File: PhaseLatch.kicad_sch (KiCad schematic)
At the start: 124 parts, among them J2 NC, J20 I_IN, J21 Q_IN, J23 CLK_IN, J5 Databus, J6 Chip select, J7 Addressbus, J8 Signals, P1 Conn_02x10_Odd_Even, P2 Conn_02x10_Odd_Even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

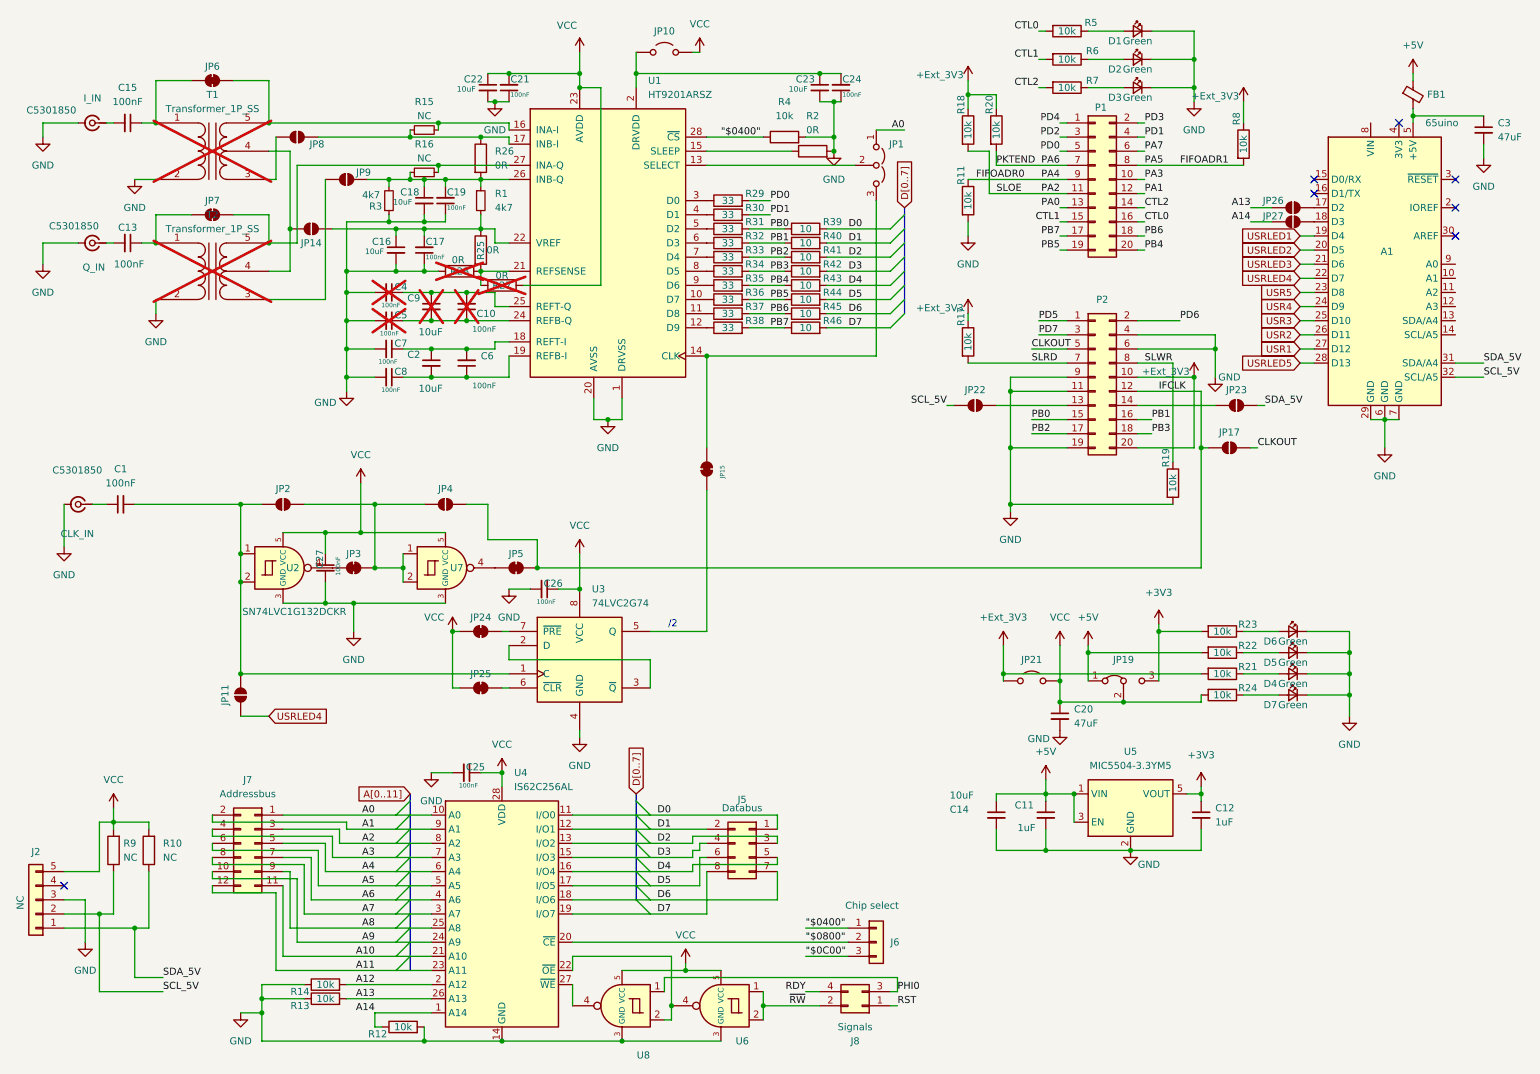
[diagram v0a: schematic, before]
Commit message: IQ bias offset, IQ balancing, documentation
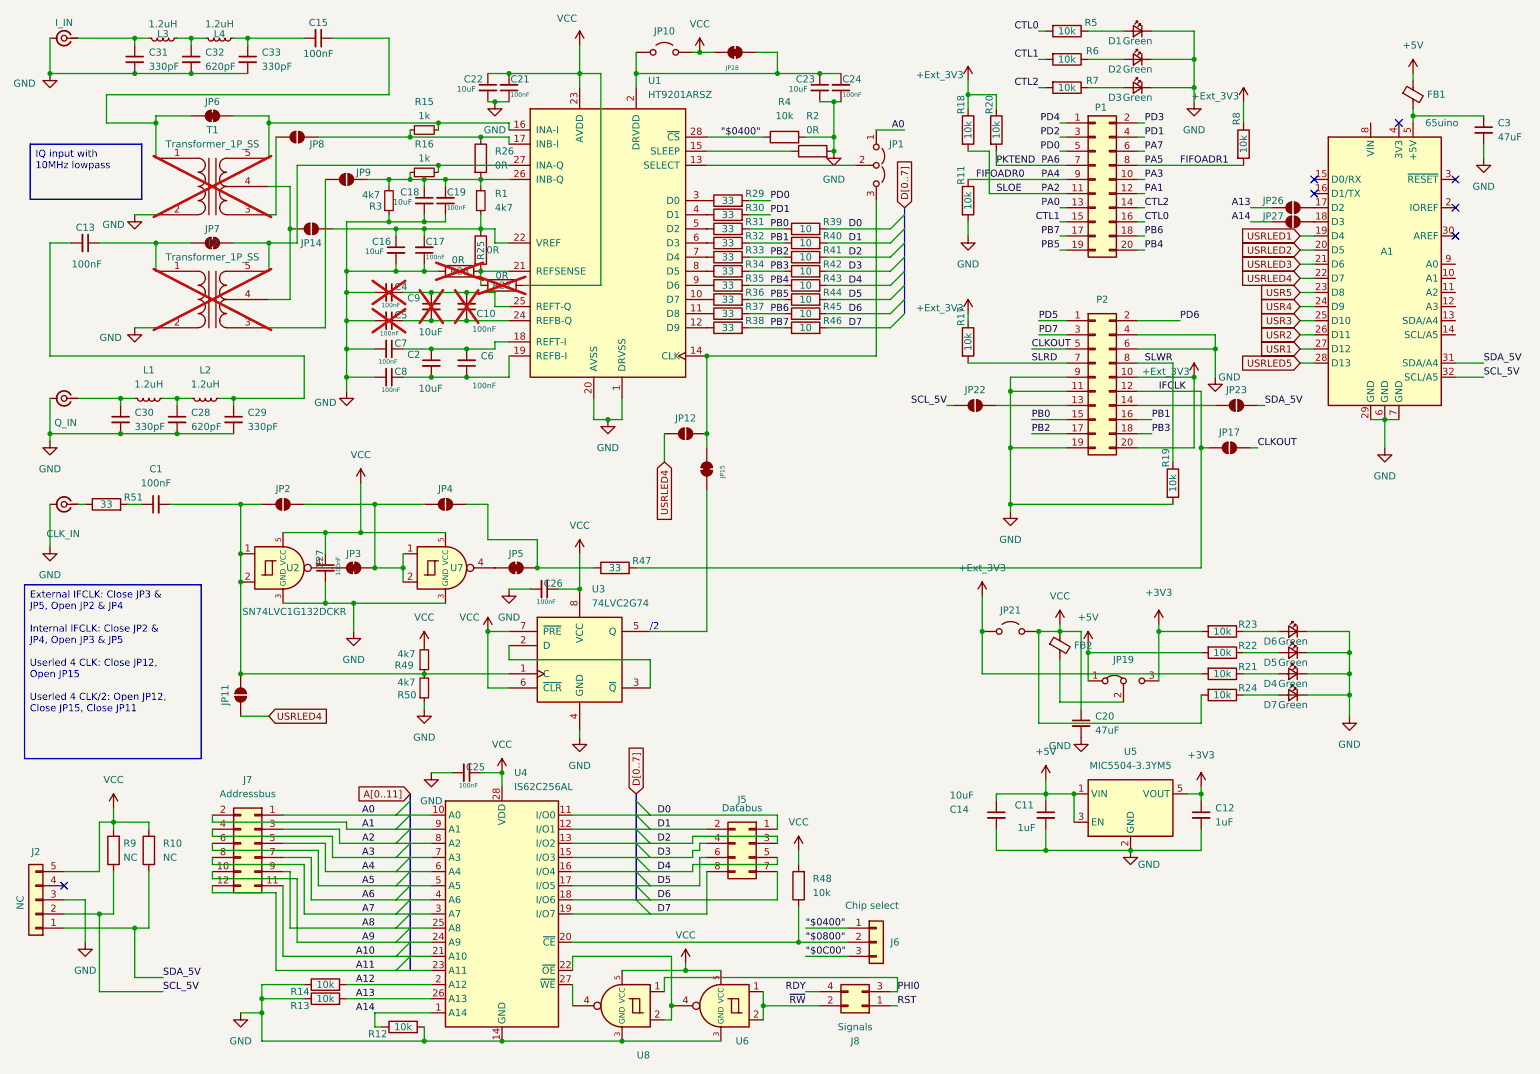
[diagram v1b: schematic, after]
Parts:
- removed JP24, JP25: ~, Jumper:SolderJumper-2_P1.3mm_Bridged_RoundedPad1.0x1.5mm, symbol Jumper:SolderJumper_2_Bridged
- added C28, C32: 620pF, Capacitor_SMD:C_0402_1005Metric, symbol Device:C_Small
- added C29, C30, C31, C33: 330pF, Capacitor_SMD:C_0402_1005Metric, symbol Device:C_Small
- added FB2: FerriteBead_Small, Inductor_SMD:L_0603_1608Metric, symbol Device:FerriteBead_Small
- added JP12: SolderJumper_2_Open, Jumper:SolderJumper-2_P1.3mm_Open_RoundedPad1.0x1.5mm, symbol Jumper:SolderJumper_2_Open
- added JP28: ~, Jumper:SolderJumper-2_P1.3mm_Bridged_RoundedPad1.0x1.5mm, symbol Jumper:SolderJumper_2_Bridged
- added L1, L2, L3, L4: 1.2uH, Inductor_SMD:L_0603_1608Metric, symbol Device:L_Small
- added R47, R51: 33, Resistor_SMD:R_0402_1005Metric, symbol Device:R
- added R48: 10k, Resistor_SMD:R_0402_1005Metric, symbol Device:R
- added R49, R50: 4k7, Resistor_SMD:R_0402_1005Metric, symbol Device:R_Small
- R15, R16: value NC -> 1k; LCSC (none) -> C11702
- U2, U6, U7, U8: LCSC C205992 -> C49188130
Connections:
- net "$0800": now also R48.1
- net GND: now also C28.2, C29.2, C30.2, C31.2, C32.2, C33.2, R50.1
- net IFCLK: now also R47.2; no longer JP4.2 (B), JP5.2 (B)
- net USRLED4: now also JP12.1 (A)
- net VCC: now also U3.6 (~{CLR}), U3.7 (~{PRE}), FB2.1, JP28.1 (A), R48.2, R49.2; no longer JP19.2 (C)
- net at J23.1 (In): now also R51.1; no longer C1.1
- net at J20.1 (In): now also C31.1, L3.2; no longer C15.2
- net at J21.1 (In): now also C30.1, L1.2; no longer C13.2
- net at C1.2, JP11.2 (B), JP2.1 (A)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: now also R49.1, R50.2
- net at C23.1, C24.2, JP10.1 (A)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: now also JP28.2 (B)
- net at JP1.3 (B), JP15.2 (B), U1.14 (CLK): now also JP12.2 (B)
- new net: C13.2, C29.1, L2.1
- new net: C1.1, R51.2
- new net: C28.1, L1.1, L2.2
- new net: JP4.2 (B), JP5.2 (B), R47.1
- new net: FB2.2, JP19.2 (C)
- new net: C32.1, L3.1, L4.2
- new net: C15.2, C33.1, L4.1
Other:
- moved on the sheet: C1, C13, C15, C20, JP21, JP6, JP7, T1, T2
